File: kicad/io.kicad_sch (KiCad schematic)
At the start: 10 parts, among them J12 LED stick, J5 IO 3x6 RA, U14 74AHCT1G125

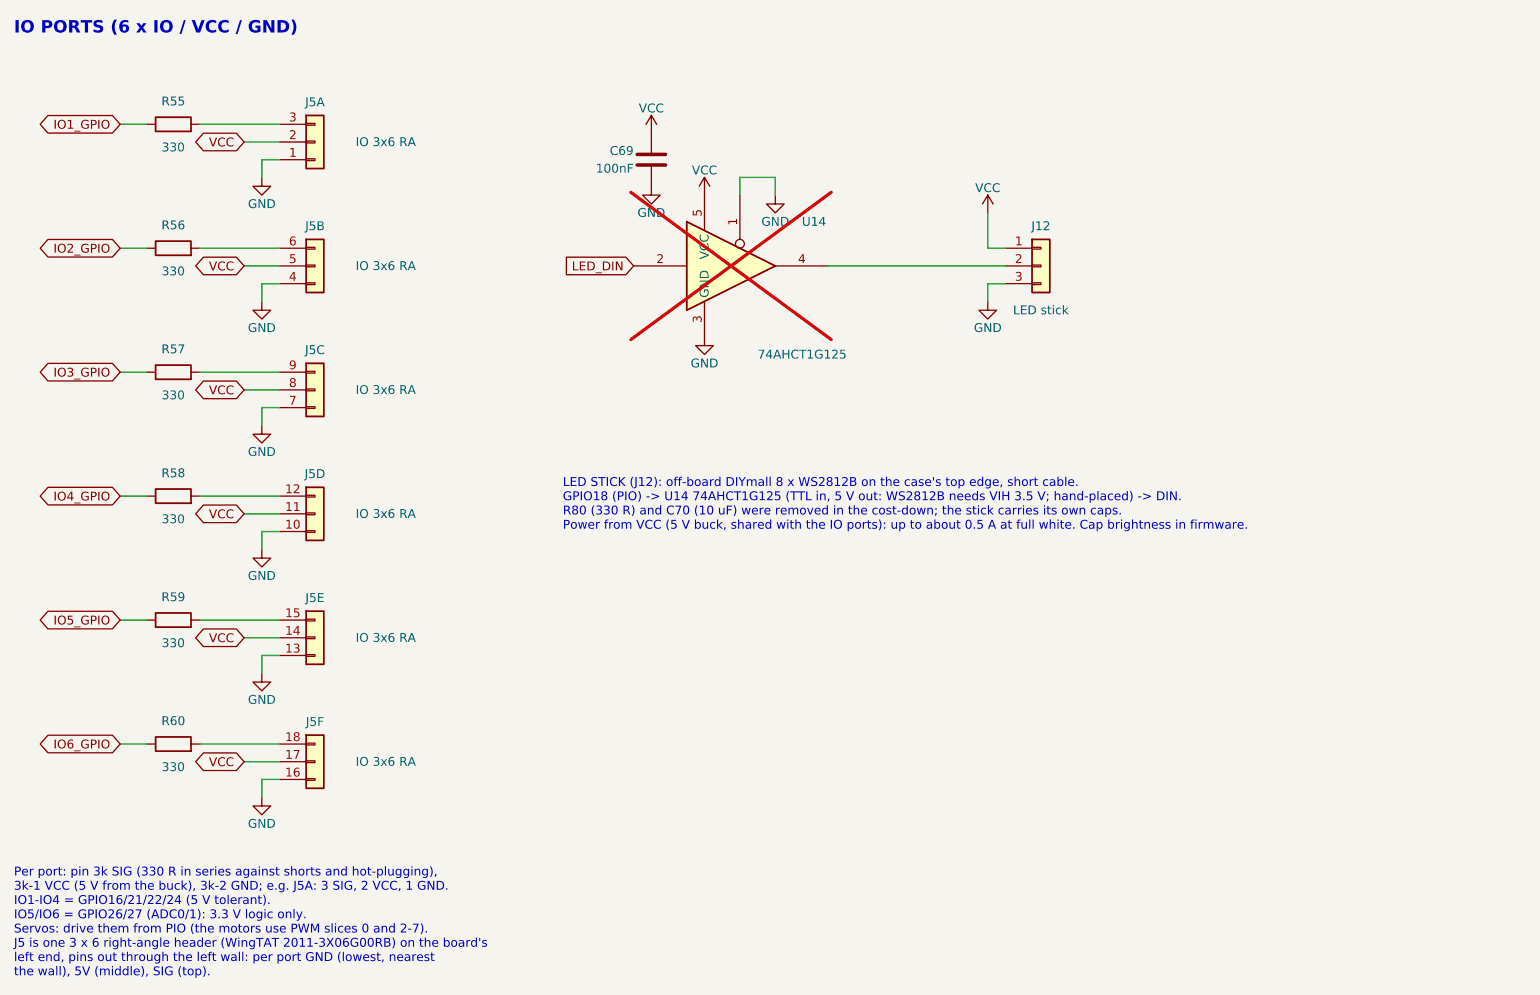
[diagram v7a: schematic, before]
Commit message: Place the brain double-sided at 66.3 x 34 mm, unrouted
- tools/place_double.py rebuilds the placement from scratch: parts on both
  sides, M1-M6 swapped to JST PH S2B-PH-K (C173752), J3 under J4, the
  switches in the bottom-right corner, the USB-C ESD and series resistors
  on the front between J1 and U10.
- Pulls in the 2026-10-20 schematic change (IO5/IO6 off the ADC pins,
  R109/R114 15k USB-A pull-downs).
- Reassigns U10 GPIOs for the new layout, keeping each motor on its own
  PWM slice and IO4-IO6 on slices 1 and 4; USB-A moves to GPIO26/27.
- Adds back-side fiducials FID4-FID6.
- The old partial autoroute is kept in kicad/reference/.

Co-Authored-By: Claude Opus 5.5 <noreply@anthropic.com>
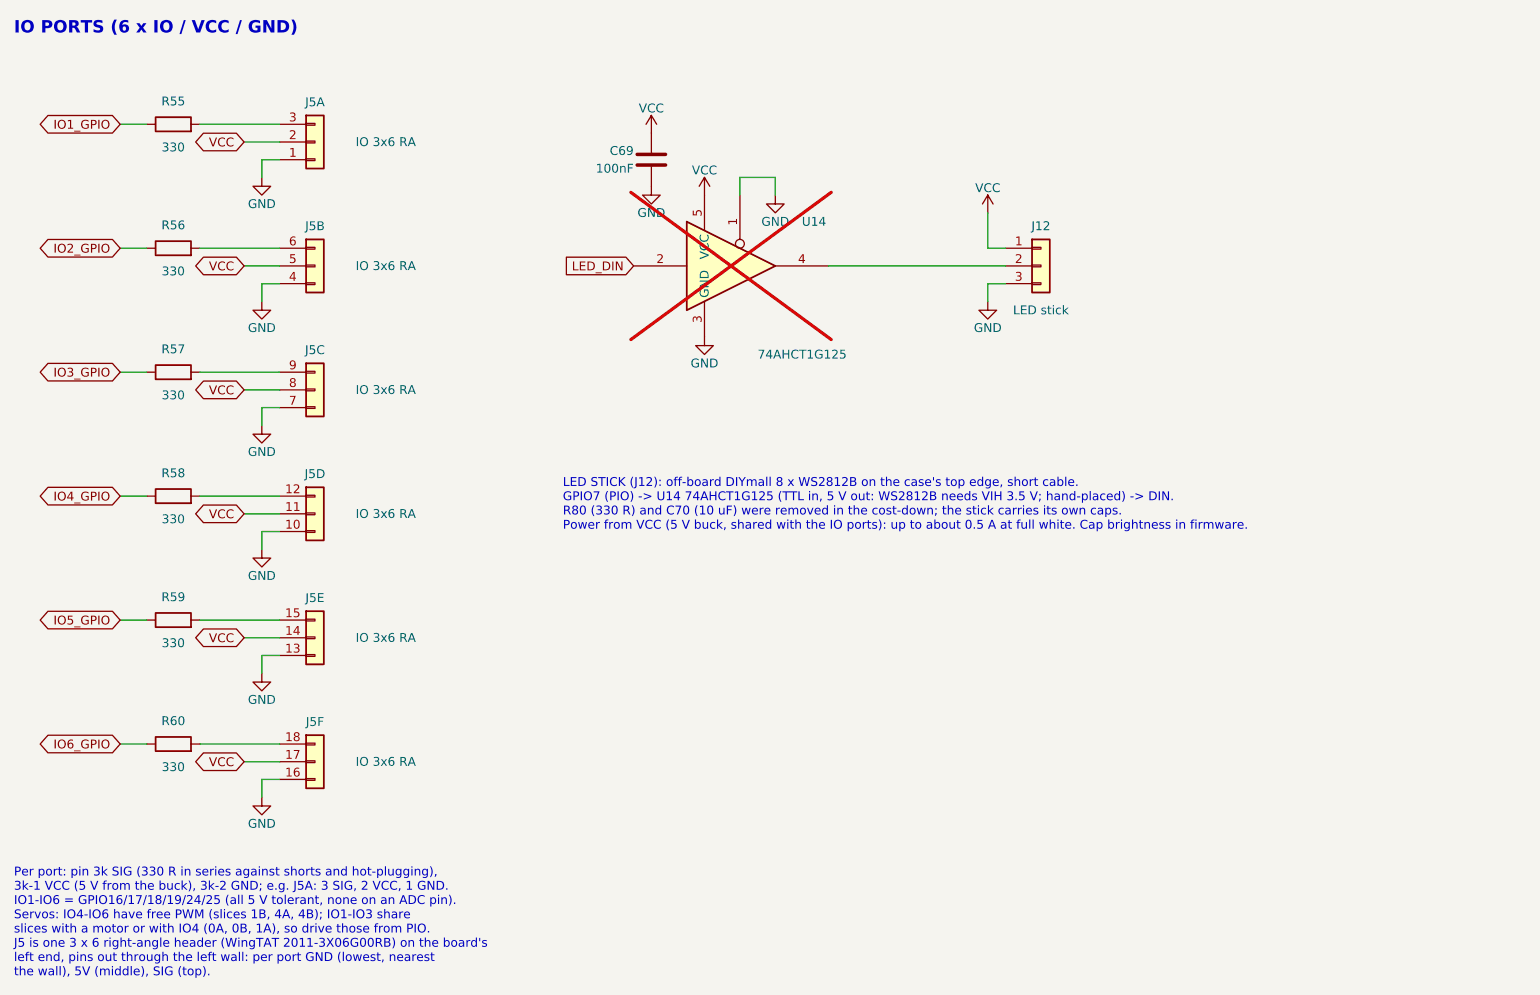
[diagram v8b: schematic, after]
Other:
- note added: "LED STICK (J12): off-board DIYmall 8 x WS2812B on the case's top edge, short cable. GPIO7 (PIO) -> U14 74AHCT1G125 (TTL in, 5 V out: WS2812B needs VIH 3.5 V; hand-placed) -> DIN. R80 (330 R) and C70 (10 uF) were removed in the cost-down; the stick carries its own caps. Power from VCC (5 V buck, shared with the IO ports): up to about 0.5 A at full white. Cap brightness in firmware."
- note added: "Per port: pin 3k SIG (330 R in series against shorts and hot-plugging), 3k-1 VCC (5 V from the buck), 3k-2 GND; e.g. J5A: 3 SIG, 2 VCC, 1 GND. IO1-IO6 = GPIO16/17/18/19/24/25 (all 5 V tolerant, none on an ADC pin). Servos: IO4-IO6 have free PWM (slices 1B, 4A, 4B); IO1-IO3 share slices with a motor or with IO4 (0A, 0B, 1A), so drive those from PIO. J5 is one 3 x 6 right-angle header (WingTAT 2011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"
- note removed: "LED STICK (J12): off-board DIYmall 8 x WS2812B on the case's top edge, short cable. GPIO18 (PIO) -> U14 74AHCT1G125 (TTL in, 5 V out: WS2812B needs VIH 3.5 V; hand-placed) -> DIN. R80 (330 R) and C70 (10 uF) were removed in the cost-down; the stick carries its own caps. Power from VCC (5 V buck, shared with the IO ports): up to about 0.5 A at full white. Cap brightness in firmware."
- note removed: "Per port: pin 3k SIG (330 R in series against shorts and hot-plugging), 3k-1 VCC (5 V from the buck), 3k-2 GND; e.g. J5A: 3 SIG, 2 VCC, 1 GND. IO1-IO4 = GPIO16/21/22/24 (5 V tolerant). IO5/IO6 = GPIO26/27 (ADC0/1): 3.3 V logic only. Servos: drive them from PIO (the motors use PWM slices 0 and 2-7). J5 is one 3 x 6 right-angle header (WingTAT 2011-3X06G00RB) on the board's left end, pins out throu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"
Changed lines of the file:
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@@
 	(generator_version "10.0")
 	(paper "A4")
-	(text "LED STICK (J12): off-board DIYmall 8 x WS2812B on the case's top edge, short cable.\nGPIO18 (PIO) -> U14 74AHCT1G125 (TTL in, 5 V out: WS2812B needs VIH 3.5 V; hand-placed) -> DIN.\nR80 (330 R) and C70 (10 uF) were removed in the cost-down; the stick carries its own caps.\nPower from VCC (5 V buck, shared with the IO ports): up to about 0.5 A at full white. Cap brightness in firmware."
+	(text "LED STICK (J12): off-board DIYmall 8 x WS2812B on the case's top edge, short cable.\nGPIO7 (PIO) -> U14 74AHCT1G125 (TTL in, 5 V out: WS2812B needs VIH 3.5 V; hand-placed) -> DIN.\nR80 (330 R) and C70 (10 uF) were removed in the cost-down; the stick carries its own caps.\nPower from VCC (5 V buck, shared with the IO ports): up to about 0.5 A at full white. Cap brightness in firmware."
 		(exclude_from_sim no)
 		(at 165.1 104.14 0)
@@
 		)
 	)
-	(text "Per port: pin 3k SIG (330 R in series against shorts and hot-plugging),\n3k-1 VCC (5 V from the buck), 3k-2 GND; e.g. J5A: 3 SIG, 2 VCC, 1 GND.\nIO1-IO4 = GPIO16/21/22/24 (5 V tolerant).\nIO5/IO6 = GPIO26/27 (ADC0/1): 3.3 V logic only.\nServos: drive them from PIO (the motors use PWM slices 0 and 2-7).\nJ5 is one 3 x 6 right-angle header (WingTAT 2011-3X06G00RB) on the board's\nleft end, pins out through the left wall: per port GND (lowest, nearest\nthe wall), 5V (middle), SIG (top)."
+	(text "Per port: pin 3k SIG (330 R in series against shorts and hot-plugging),\n3k-1 VCC (5 V from the buck), 3k-2 GND; e.g. J5A: 3 SIG, 2 VCC, 1 GND.\nIO1-IO6 = GPIO16/17/18/19/24/25 (all 5 V tolerant, none on an ADC pin).\nServos: IO4-IO6 have free PWM (slices 1B, 4A, 4B); IO1-IO3 share\nslices with a motor or with IO4 (0A, 0B, 1A), so drive those from PIO.\nJ5 is one 3 x 6 right-angle header (WingTAT 2011-3X06G00RB) on the board's\nleft end, pins out through the left wall: per port GND (lowest, nearest\nthe wall), 5V (middle), SIG (top)."
 		(exclude_from_sim no)
 		(at 86.36 152.4 0)
